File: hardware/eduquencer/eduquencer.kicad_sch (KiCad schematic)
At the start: 2 parts

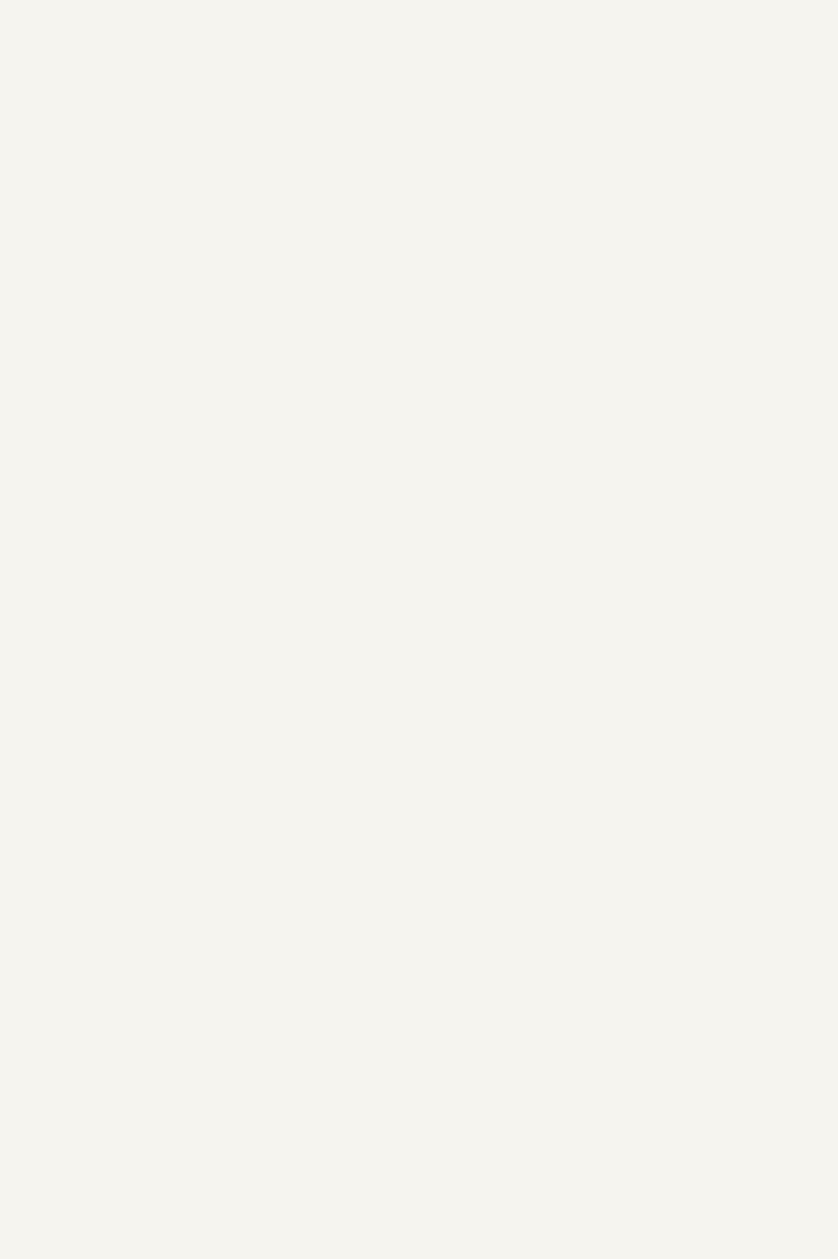
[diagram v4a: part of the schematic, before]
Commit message: add preliminary led circuit
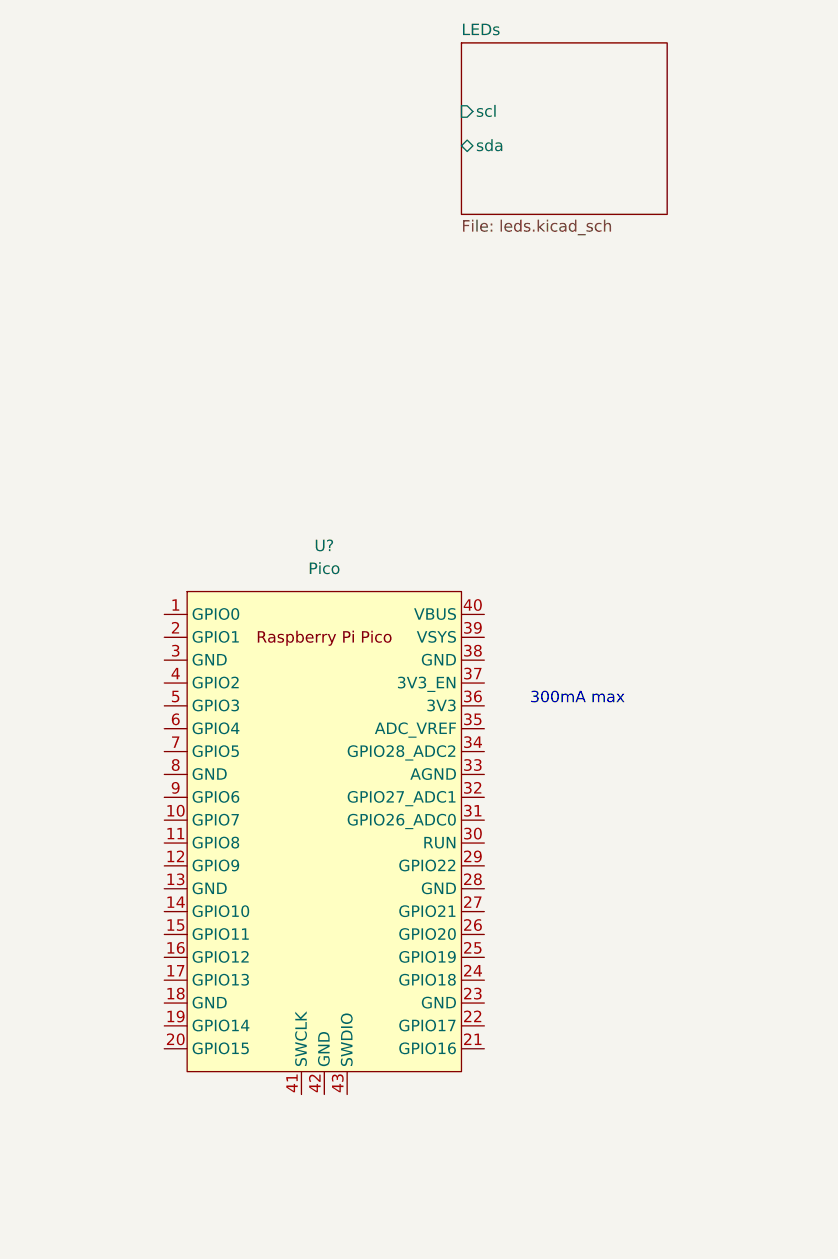
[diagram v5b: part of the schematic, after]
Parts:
- added U?: Pico, RaspberryPi-Pico:RPi_Pico_SMD_TH, symbol MCU_RaspberryPi_and_Boards:Pico
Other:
- added sheet LEDs (leds.kicad_sch)
- note added: "300mA max"
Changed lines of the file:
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@@
     (stroke (width 0) (type default) (color 0 0 0 0))
+  )
+  (text "300mA max" (at 160.02 97.79 0)
+    (effects (font (size 1.27 1.27)) (justify left bottom))
   )
   (global_label "spi0_cs" (shape input) (at 236.22 43.18 180) (fields_autoplaced)
@@
     )
     (pin "1")
+  )
+  (symbol (lib_id "MCU_RaspberryPi_and_Boards:Pico") (at 137.16 111.76 0) (unit 1)
+    (in_bom yes) (on_board yes) (fields_autoplaced)
+    (property "Reference" "U?" (id 0) (at 137.16 80.01 0))
+    (property "Value" "Pico" (id 1) (at 137.16 82.55 0))
+    (property "Footprint" "RaspberryPi-Pico:RPi_Pico_SMD_TH" (id 2) (at 137.16 111.76 90)
+      (effects (font (size 1.27 1.27)) hide)
+    )
+    (property "Datasheet" "" (id 3) (at 137.16 111.76 0)
+      (effects (font (size 1.27 1.27)) hide)
+    )
+    (pin "1")
+    (pin "10")
+    (pin "11")
+    (pin "12")
+    (pin "13")
+    (pin "14")
+    (pin "15")
+    (pin "16")
+    (pin "17")
+    (pin "18")
+    (pin "19")
+    (pin "2")
+    (pin "20")
+    (pin "21")
+    (pin "22")
+    (pin "23")
+    (pin "24")
+    (pin "25")
+    (pin "26")
+    (pin "27")
+    (pin "28")
+    (pin "29")
+    (pin "3")
+    (pin "30")
+    (pin "31")
+    (pin "32")
+    (pin "33")
+    (pin "34")
+    (pin "35")
+    (pin "36")
+    (pin "37")
+    (pin "38")
+    (pin "39")
+    (pin "4")
+    (pin "40")
+    (pin "41")
+    (pin "42")
+    (pin "43")
+    (pin "5")
+    (pin "6")
+    (pin "7")
+    (pin "8")
+    (pin "9")
   )
   (symbol (lib_id "SN74AHCT244NSR:SN74AHCT244NSR") (at 35.56 86.36 0) (unit 1)
@@
     )
   )
+  (sheet (at 152.4 24.13) (size 22.86 19.05) (fields_autoplaced)
+    (stroke (width 0.1524) (type solid) (color 0 0 0 0))
+    (fill (color 0 0 0 0.0000))
+    (property "Sheet name" "LEDs" (id 0) (at 152.4 23.4184 0)
+      (effects (font (size 1.27 1.27)) (justify left bottom))
+    )
+    (property "Sheet file" "leds.kicad_sch" (id 1) (at 152.4 43.7646 0)
+      (effects (font (size 1.27 1.27)) (justify left top))
+    )
+    (pin "scl" input (at 152.4 31.75 180)
+      (effects (font (size 1.27 1.27)) (justify left))
+    )
+    (pin "sda" bidirectional (at 152.4 35.56 180)
+      (effects (font (size 1.27 1.27)) (justify left))
+    )
+  )
   (sheet (at 236.22 33.02) (size 31.75 22.86) (fields_autoplaced)
     (stroke (width 0) (type solid) (color 0 0 0 0))
@@
   (sheet_instances
     (path "/" (page "1"))
+    (path "/5b8fece9-be36-46a7-9d0e-2ff3cd7cbc98" (page "5"))
     (path "/3ea32a21-cebb-4ee4-9c8c-55bda166121d" (page "7"))
     (path "/45a0ea3a-da06-4958-b002-46f0015400cc" (page "8"))
@@
       (reference "#PWR?") (unit 1) (value "VCC") (footprint "")
     )
+    (path "/5b8fece9-be36-46a7-9d0e-2ff3cd7cbc98/7c726f5c-48d2-4208-a96c-9712233e03a3"
+      (reference "#PWR?") (unit 1) (value "+3V3") (footprint "")
+    )
     (path "/45a0ea3a-da06-4958-b002-46f0015400cc/9d10644a-09de-4a82-8225-d83054f5420c"
       (reference "#PWR?") (unit 1) (value "GND") (footprint "")
@@
       (reference "#PWR?") (unit 1) (value "GND") (footprint "")
     )
+    (path "/5b8fece9-be36-46a7-9d0e-2ff3cd7cbc98/f730121f-8b6c-4633-b087-6e98b0e7037f"
+      (reference "#PWR?") (unit 1) (value "GND") (footprint "")
+    )
     (path "/3ea32a21-cebb-4ee4-9c8c-55bda166121d/00000000-0000-0000-0000-00005fccac86"
       (reference "C?") (unit 1) (value "100n") (footprint "Capacitor_SMD:C_0603_1608Metric")
@@
       (reference "C?") (unit 1) (value "22p") (footprint "Capacitor_SMD:C_0603_1608Metric")
     )
+    (path "/5b8fece9-be36-46a7-9d0e-2ff3cd7cbc98/3835009f-bcd8-41ea-b8e5-77d89ce656d1"
+      (reference "C?") (unit 1) (value "100n") (footprint "Capacitor_SMD:C_0603_1608Metric")
+    )
     (path "/483a9fb8-34c0-4322-aa23-27a5733d4158"
       (reference "C?") (unit 1) (value "100n") (footprint "Capacitor_SMD:C_0603_1608Metric")
@@
       (reference "IC?") (unit 1) (value "SN74AHCT244NSR") (footprint "SOIC127P780X200-20N")
     )
+    (path "/5b8fece9-be36-46a7-9d0e-2ff3cd7cbc98/cf3742b4-b0be-438f-9d82-b93682463e29"
+      (reference "IC?") (unit 1) (value "MCP23018-E_SO") (footprint "SOIC127P1030X265-28N")
+    )
     (path "/45a0ea3a-da06-4958-b002-46f0015400cc/00000000-0000-0000-0000-00005fdff083"
       (reference "J?") (unit 1) (value "Eurorack PWR") (footprint "Connector_IDC:IDC-Header_2x05_P2.54mm_Vertical")
@@
       (reference "L?") (unit 1) (value "10u") (footprint "Inductor_SMD:L_0805_2012Metric")
     )
+    (path "/5b8fece9-be36-46a7-9d0e-2ff3cd7cbc98/0c386859-abb1-4d41-b542-f79dff07f43c"
+      (reference "LED?") (unit 1) (value "XZMYK45WT-9") (footprint "XZMYK45WT9")
+    )
+    (path "/5b8fece9-be36-46a7-9d0e-2ff3cd7cbc98/10dfb550-44b4-45bc-96ef-6994a952ed80"
+      (reference "LED?") (unit 1) (value "XZMYK45WT-9") (footprint "XZMYK45WT9")
+    )
+    (path "/5b8fece9-be36-46a7-9d0e-2ff3cd7cbc98/5483821c-f480-431e-940c-69c1cf7e33ba"
+      (reference "LED?") (unit 1) (value "XZMYK45WT-9") (footprint "XZMYK45WT9")
+    )
+    (path "/5b8fece9-be36-46a7-9d0e-2ff3cd7cbc98/558792d4-69a8-40a4-8c89-21dd89fde384"
+      (reference "LED?") (unit 1) (value "XZMYK45WT-9") (footprint "XZMYK45WT9")
+    )
+    (path "/5b8fece9-be36-46a7-9d0e-2ff3cd7cbc98/87f80e4c-b247-4252-9f7c-9724559d1951"
+      (reference "LED?") (unit 1) (value "XZMYK45WT-9") (footprint "XZMYK45WT9")
+    )
+    (path "/5b8fece9-be36-46a7-9d0e-2ff3cd7cbc98/8906d63d-ab9f-496c-9d2a-573fdf9f5944"
+      (reference "LED?") (unit 1) (value "XZMYK45WT-9") (footprint "XZMYK45WT9")
+    )
+    (path "/5b8fece9-be36-46a7-9d0e-2ff3cd7cbc98/a2498c7e-af7e-46db-8363-fe05f42f106e"
+      (reference "LED?") (unit 1) (value "XZMYK45WT-9") (footprint "XZMYK45WT9")
+    )
+    (path "/5b8fece9-be36-46a7-9d0e-2ff3cd7cbc98/a417f516-45c1-44ea-a482-9f4def1aac3b"
+      (reference "LED?") (unit 1) (value "XZMYK45WT-9") (footprint "XZMYK45WT9")
+    )
+    (path "/5b8fece9-be36-46a7-9d0e-2ff3cd7cbc98/a908c14e-8db0-43d6-ad9e-7bc7cd7d2260"
+      (reference "LED?") (unit 1) (value "XZMYK45WT-9") (footprint "XZMYK45WT9")
+    )
+    (path "/5b8fece9-be36-46a7-9d0e-2ff3cd7cbc98/ac0d2d6d-98f5-43cb-84e1-62fede006b4b"
+      (reference "LED?") (unit 1) (value "XZMYK45WT-9") (footprint "XZMYK45WT9")
+    )
+    (path "/5b8fece9-be36-46a7-9d0e-2ff3cd7cbc98/c7222b6a-06a9-4042-b6f2-a18043608bdc"
+      (reference "LED?") (unit 1) (value "XZMYK45WT-9") (footprint "XZMYK45WT9")
+    )
+    (path "/5b8fece9-be36-46a7-9d0e-2ff3cd7cbc98/cf78c488-1611-40a0-85fa-15bfae75637e"
+      (reference "LED?") (unit 1) (value "XZMYK45WT-9") (footprint "XZMYK45WT9")
+    )
+    (path "/5b8fece9-be36-46a7-9d0e-2ff3cd7cbc98/cfa4937b-26f6-46da-bfe2-415fd70d9280"
+      (reference "LED?") (unit 1) (value "XZMYK45WT-9") (footprint "XZMYK45WT9")
+    )
+    (path "/5b8fece9-be36-46a7-9d0e-2ff3cd7cbc98/d5e787ca-6648-4801-8007-94f763b9aa79"
+      (reference "LED?") (unit 1) (value "XZMYK45WT-9") (footprint "XZMYK45WT9")
+    )
+    (path "/5b8fece9-be36-46a7-9d0e-2ff3cd7cbc98/e4bba691-bbd2-4759-8c9f-7724c35e6d7a"
+      (reference "LED?") (unit 1) (value "XZMYK45WT-9") (footprint "XZMYK45WT9")
+    )
+    (path "/5b8fece9-be36-46a7-9d0e-2ff3cd7cbc98/f6959a67-8719-49d3-9608-8ec7cdb63e2f"
+      (reference "LED?") (unit 1) (value "XZMYK45WT-9") (footprint "XZMYK45WT9")
+    )
     (path "/3ea32a21-cebb-4ee4-9c8c-55bda166121d/00000000-0000-0000-0000-00005fcfec8f"
       (reference "R?") (unit 1) (value "36k") (footprint "Resistor_SMD:R_0603_1608Metric")
@@
       (reference "U?") (unit 1) (value "LM4040DBZ-5") (footprint "Package_TO_SOT_SMD:SOT-23")
     )
-  )
+    (path "/780076de-fb73-43f2-b5aa-1c95059ff25d"
+      (reference "U?") (unit 1) (value "Pico") (footprint "RaspberryPi-Pico:RPi_Pico_SMD_TH")
+    )
+  )

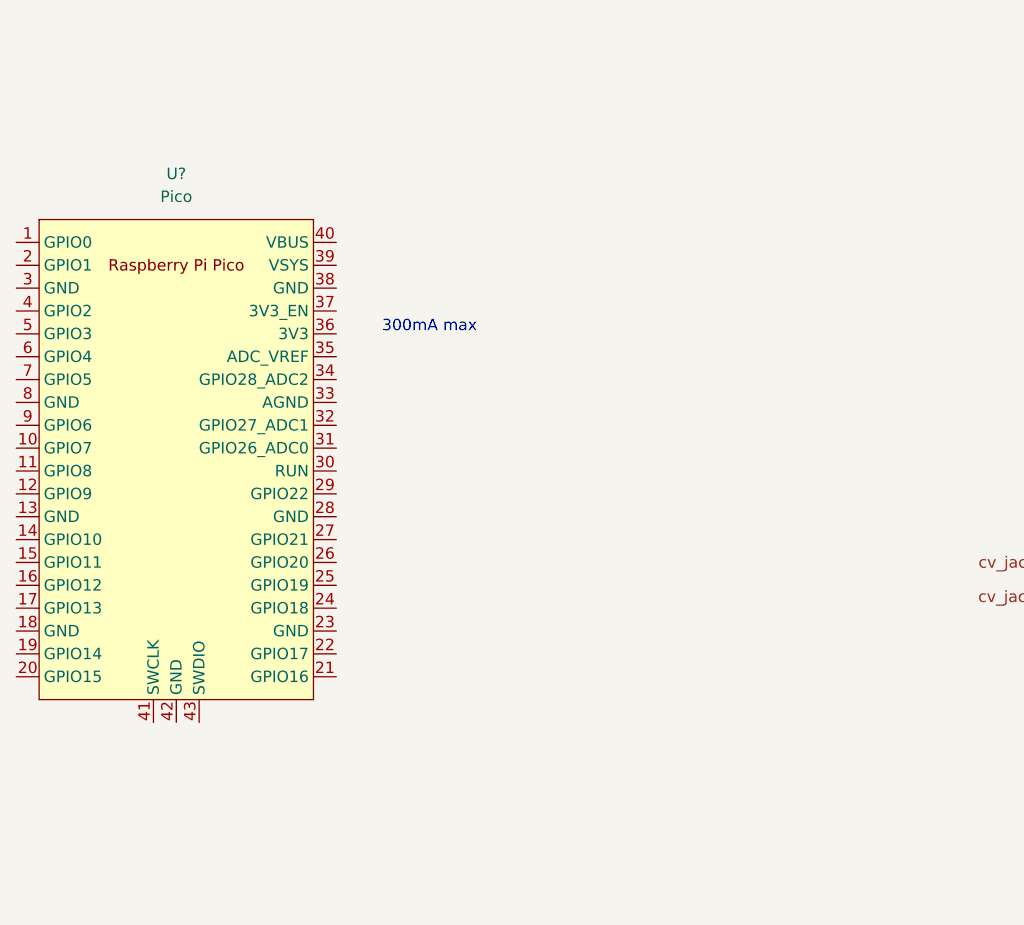
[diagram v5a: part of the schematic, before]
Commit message: CV in conditioning circuits
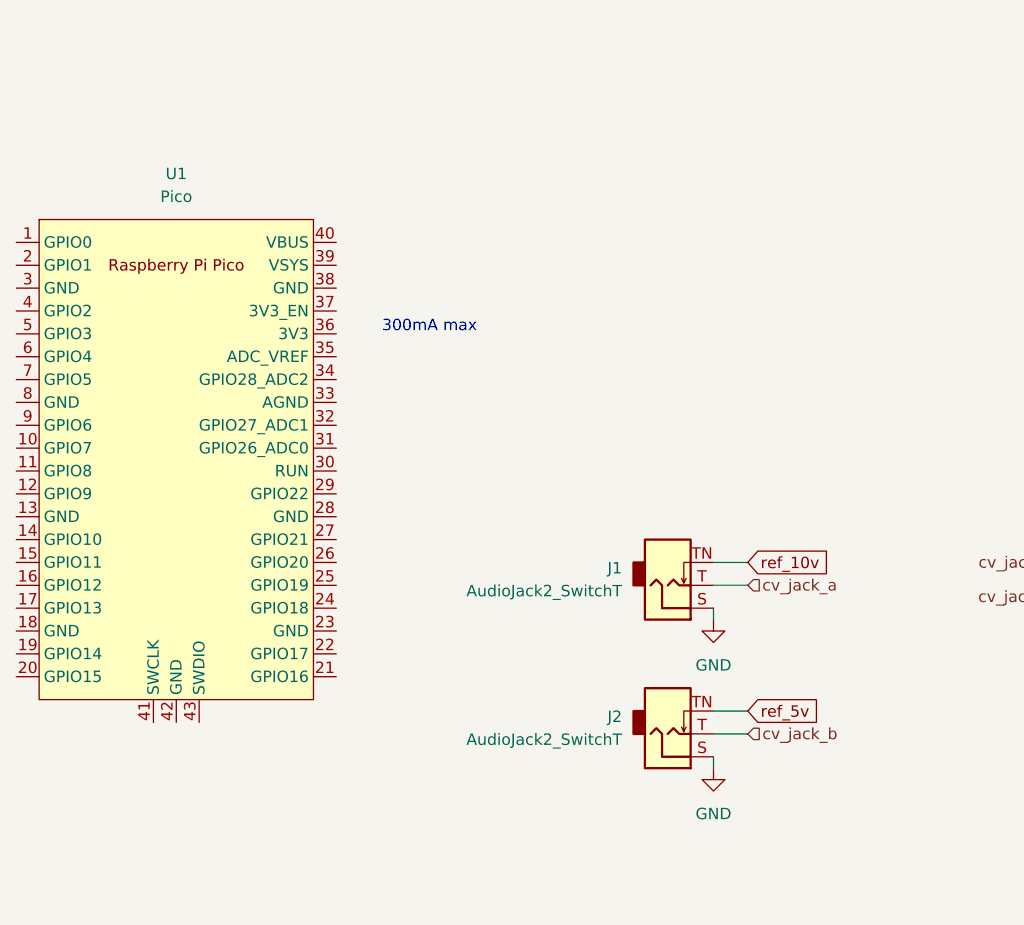
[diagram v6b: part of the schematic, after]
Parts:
- added J1, J2: AudioJack2_SwitchT, symbol Connector:AudioJack2_SwitchT
- gave numbers to parts that had none: 1
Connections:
- net GND: now also J1.S, J2.S
- net cv_jack_a: now also J1.T
- net cv_jack_b: now also J2.T
- new net ref_10v: J1.TN
- new net ref_5v: J2.TN
